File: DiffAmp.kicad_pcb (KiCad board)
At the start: 2 copper layers, 99.7 x 35.6 mm, 272 parts, among them J1 USB_OTG, J2 Screw_Terminal_1x03, J3 Conn_01x02, J4 Conn_01x02, J5 Conn_01x02, U1 SF_IHXXXXS, U2 TPS7A49, U3 TPS7A30, U4 OPA189, U5 AD8421, U6 OPA189, U7 OPA189

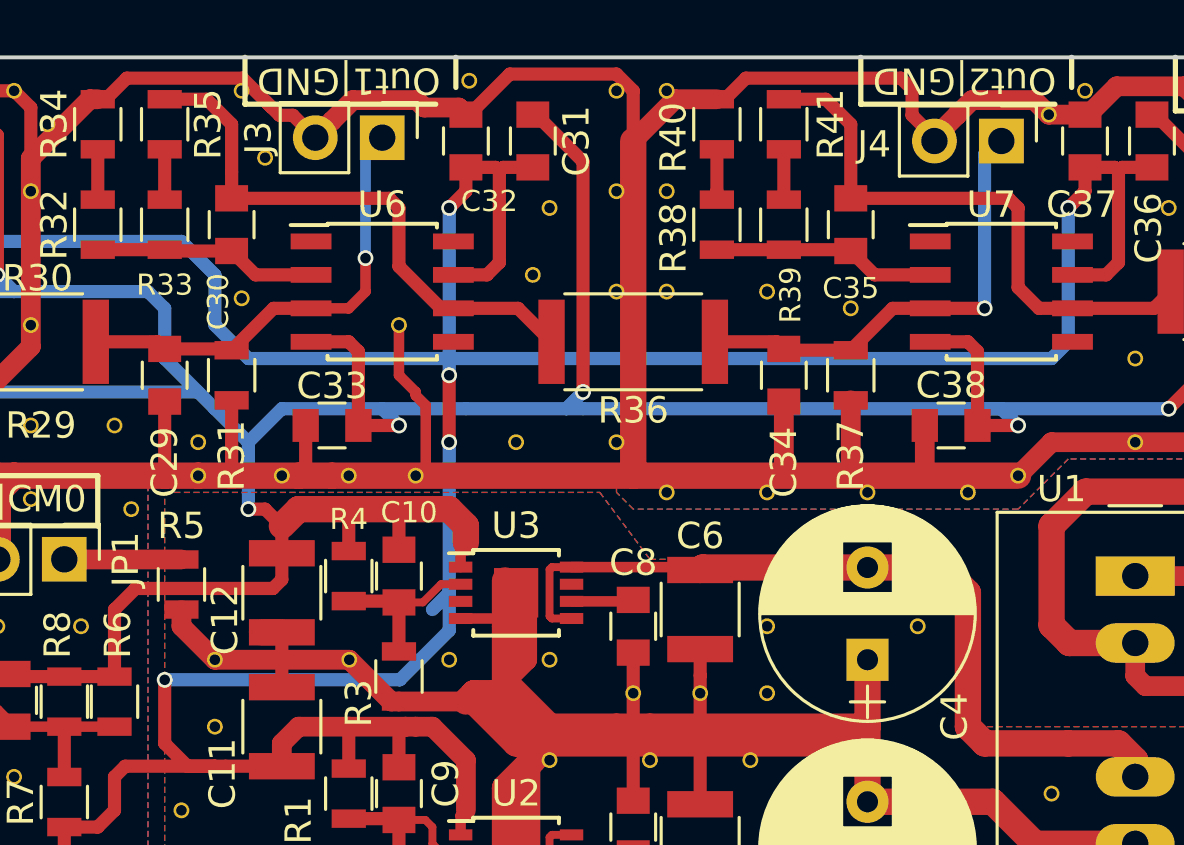
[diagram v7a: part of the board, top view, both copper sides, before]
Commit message: Small modifications to layout - GND-Plane, VDD/VSS routing
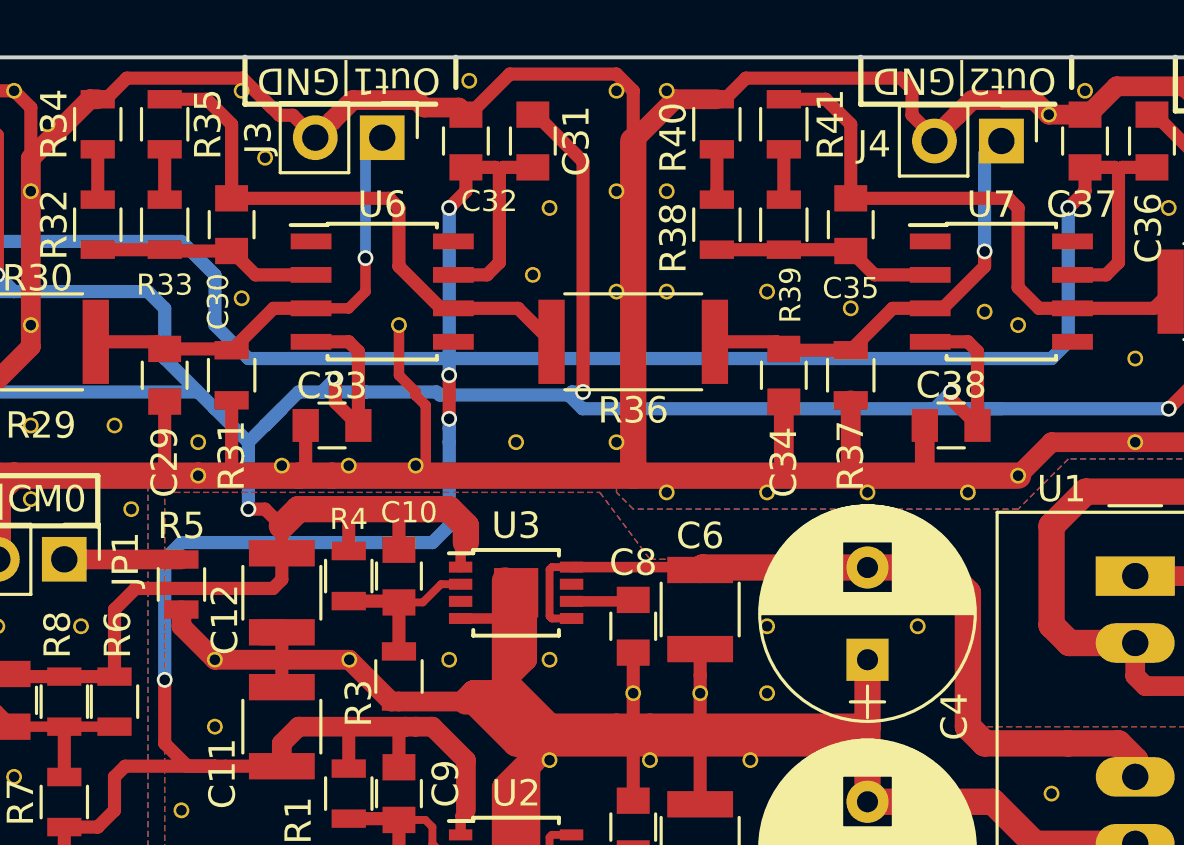
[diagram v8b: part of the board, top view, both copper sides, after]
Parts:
- added ?: , DiffAmp:VIA-0.6mm, F.Cu at (96.5, 29.2)
- added ?: , DiffAmp:VIA-0.6mm, F.Cu at (95.2, 28.7)
- moved ? 0.38 mm to (71.1, 34.5)
- moved ? 0.38 mm to (68.6, 34.5)
- moved ? 0.38 mm to (73.7, 34.5)
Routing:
- net VSSA: track 198.9 -> 200.7 mm
- net /Diff-Amp & Gain Stages/OutSt1: track 17.8 -> 16.8 mm
- net VDDA: track 193.5 -> 192.6 mm
